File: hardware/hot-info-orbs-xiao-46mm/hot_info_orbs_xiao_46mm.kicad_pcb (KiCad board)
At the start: 2 copper layers, 224 x 47.8 mm, 13 parts, among them SW1 SW_Push, SW2 SW_Push, SW3 SW_Push, U2 XIAO ESP32-S3 Plus

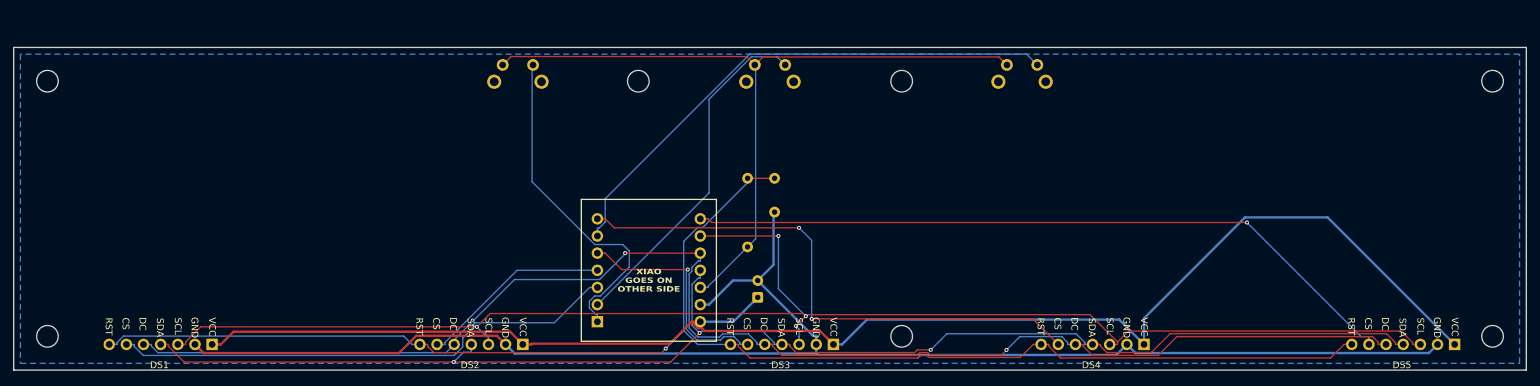
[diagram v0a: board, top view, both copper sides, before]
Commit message: 46 mm board rev 2.1: grown 5 mm at the top, posts on all seven holes
Placed in the Fusion overall assembly, the X0.2 board's top mounting holes
sat under the enclosure's top lip, so the top row hung from corner hangers.
Rejected shifting the board up: the displays are pinned by the bezel holes
and would move with it. Rejected keeping the hangers: Scott wants a post at
either end. So tools/grow_top.py grows the TOP edge 5 mm (the sockets fix
the bottom), moves the top-row holes, SW1-3 and labels with it, and the
board is re-routed from bare copper (300 tracks+vias, DRC clean).

Rev silk is 2.1 (Scott's number); it read X0.3 for a few minutes and that
zip was discarded, never ordered. fab/ gets a 2.1_run1 zip; the X0.2 zip
stays as the record and is marked superseded.

Fusion: main_body_front v4 (O6 posts + O2.9 pins on all seven holes,
hangers deleted, one body), overall assembly v4 (rev 2.1 STEP on the bezel
holes, xref refreshed). Interference enclosure vs PCB / display 5 clean.

TRAPS: the fusion-essentials active document flips between calls and reads
answer about the wrong doc; grow the edge, don't shift the board; KiCad
text must be set via pcbnew so the render_cache regenerates.

Co-Authored-By: Claude Fable 5.1 <noreply@anthropic.com>
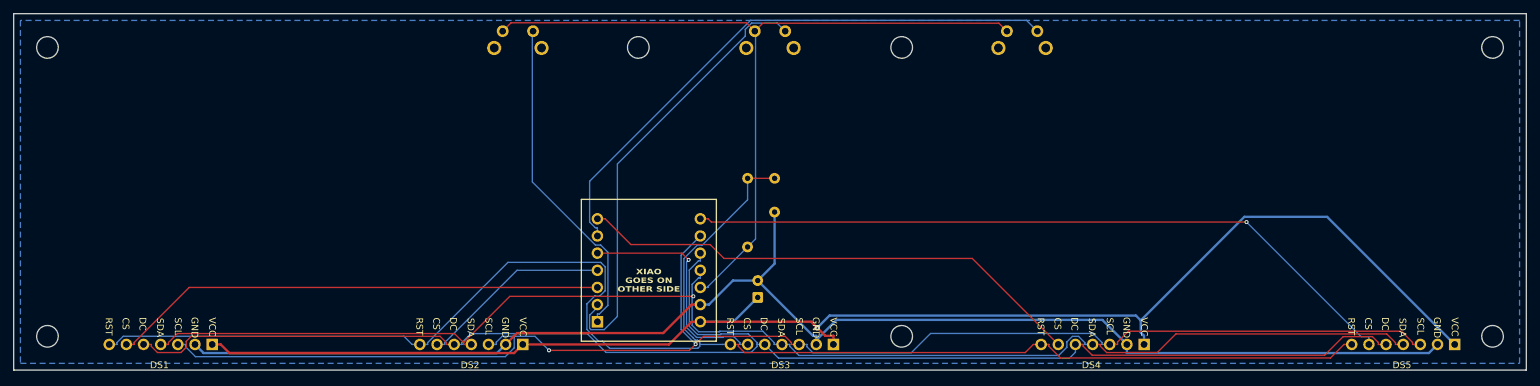
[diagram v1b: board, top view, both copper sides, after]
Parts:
- moved SW1 5.00 mm to (114.0, 59.6)
- moved SW2 5.00 mm to (151.3, 59.6)
- moved SW3 5.00 mm to (188.6, 59.6)
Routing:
- net /RST: track 222.9 -> 242.8 mm, vias 1 -> 0
- net GND: track 224.3 -> 209.4 mm
- net /SW2: track 51.6 -> 66.1 mm
- net /SCLK: track 224.8 -> 216.9 mm, vias 4 -> 2
- net /CS4: track 82.8 -> 76.0 mm, vias 2 -> 0
- net /SW3: track 79.7 -> 85.6 mm
- net /DC: track 211.9 -> 217.5 mm, vias 2 -> 0
- net /3V3: track 113.7 -> 118.7 mm
- net /CS1: track 75.8 -> 73.4 mm
- net /MOSI: track 208.1 -> 205.9 mm, vias 3 -> 1
- net /SW1: track 50.1 -> 49.0 mm
- net +5V: track 220.5 -> 220.0 mm, vias 0 -> 1
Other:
- board size 224 x 47.8 mm -> 224 x 52.8 mm
- board text added: "XIAO ESP32-S3 · rev 2.1 · 46 mm pitch"
- board text removed: "XIAO ESP32-S3 · rev X0.2 · 46 mm pitch"

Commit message: 46 mm board rev 2.3: XIAO 4 mm toward the bottom edge, passives beside it
Scott wants the USB-C jack as close to the enclosure wall as the board
allows without growing it or crowding the pins. tools/lower_xiao.py drops
U2 4.0 mm (the top of his 2-4 mm estimate): pad copper 2.31 mm from the
edge against a 0.5 rule, socket housings 1.9 mm inside it, USB-C face
0.6 mm past it. Rejected 2.73 mm (USB face flush with the edge, no silk
warnings) because the ask was "as much as possible"; the 3 warnings are
the footprint's own USB-C silk crossing the edge, which the fab trims.

C1 could not follow: DS3's back-side pin labels sit at y 101.9 and C1 was
already against them, so a 2.4 mm drop landed its 5V pad on the "DC"
label. It moves 3.2 mm sideways instead, courtyard 0.5 mm from the XIAO
socket, giving up the speculative castellation-pad margin. The 5V run is
9.25 mm pad to pad, the same as 2.1. C2 and R1 swap into one column above
C1, RST pads adjacent, so the long run is the 3V3 feed.

Re-routed from bare copper (284 tracks+vias, 0 unrouted), DRC 0 errors /
0 unconnected / 0 parity. New 2.3_run1 zip; the 2.1 zip stays as the
record. STEP overwritten in place, so the Fusion USB cutout built on 2.1
is 4 mm off until re-imported (noted in docs/ENCLOSURE.md). There is no
2.2. route_xiao.py now reruns Freerouting on a "stage interrupted" pass
with a non-empty SES, which its empty-file check missed.

Co-Authored-By: Claude Fable 5.1 <noreply@anthropic.com>
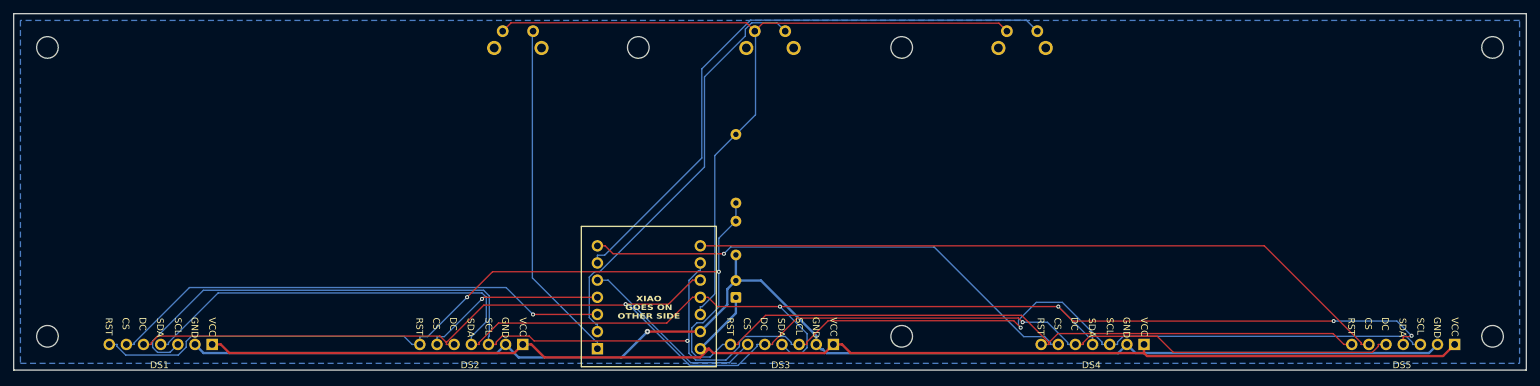
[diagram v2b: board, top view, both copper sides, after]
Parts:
- moved R1 16.8 mm to (144.0, 74.9), turned to -90 degrees
- moved C2 8.55 mm to (144.0, 87.7)
- moved U2 4.00 mm to (131.1, 99.0)
- moved C1 3.23 mm to (144.0, 99.0)
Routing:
- net /MOSI: track 205.9 -> 227.1 mm, vias 1 -> 4
- net +5V: track 220.0 -> 200.9 mm, vias 1 -> 0
- net /SCLK: track 216.9 -> 231.1 mm
- net /RST: track 242.8 -> 228.7 mm, vias 0 -> 2
- net GND: track 209.4 -> 202.5 mm, vias 0 -> 1
- net /CS3: track 34.4 -> 28.4 mm, vias 1 -> 0
- net /DC: track 217.5 -> 212.5 mm, vias 0 -> 2
- net /SW2: track 66.1 -> 62.3 mm
- net /SW3: track 85.6 -> 89.1 mm
- net /3V3: track 118.7 -> 122.2 mm
- net /SW1: track 49.0 -> 51.2 mm
- net /CS5: track 107.4 -> 105.2 mm, vias 1 -> 0
- net /CS1: track 73.4 -> 75.0 mm, vias 0 -> 1
- net /CS2: track 28.5 -> 27.3 mm, vias 0 -> 1
- net /CS4: track 76.0 -> 75.3 mm, vias 0 -> 1
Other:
- board text added: "XIAO ESP32-S3 · rev 2.3 · 46 mm pitch"
- board text removed: "XIAO ESP32-S3 · rev 2.1 · 46 mm pitch"

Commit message: 46 mm board rev 2.3 run 2: front GND pour + stitching vias in the two back-pour islands
Scott spotted two wide bare bands in the back pour (SW2 down past R1 to
the XIAO; DS1 to DS2 along the bottom edge). Measured with the fill redone
in memory and island removal off: removed islands of 283 and 211 mm2,
copper closed in by the SW2/SW3 pair and the 3V3 feed, and by the DS1
CS1/SCLK/MOSI bundle and the shared RST track. Removing them is correct,
so the fix is a connection: tools/stitch_islands.py puts a 0.8/0.3 GND via
in each island and pours the GND zone on F.Cu too.

Rejected "two vias only" (asked for, tried first): with no front copper the
island plus via is still floating and KiCad removes it again, DRC calls the
vias dangling. Rejected a front track from each via to a socket GND pin:
it would have to skirt the pin rows, and a front pour is normal on a
two-layer board. The front pour starves DS5's GND thermal to one spoke
(the +5V front track along the bottom runs under DS5 only); that pad's
spokes are turned 45 degrees on the board instance, rejected a solid
connection (hand soldering) and rerouting (everything would move).

DRC 0 errors / 3 warnings (USB-C silk over the edge, as before) / 0
unconnected / 0 parity. 16 vias. New zip 2.3_run2; run1 kept as the record
of the back-pour-only layout, not to be sent.

Co-Authored-By: Claude Fable 5.1 <noreply@anthropic.com>
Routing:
- net GND: vias 1 -> 3
- added copper zone on F.Cu, net GND
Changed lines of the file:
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@@
 			(remove_unused_layers no)
 			(net "GND")
+			(thermal_bridge_angle 45)
 		)
 		(pad "3" thru_hole oval
@@
 	)
 	(via
+		(at 68.699813 101.4584)
+		(size 0.8)
+		(drill 0.3)
+		(layers "F.Cu" "B.Cu")
+		(net "GND")
+	)
+	(via
+		(at 143.100652 68.130134)
+		(size 0.8)
+		(drill 0.3)
+		(layers "F.Cu" "B.Cu")
+		(net "GND")
+	)
+	(via
 		(at 130.8936 104.08)
 		(size 0.8)
@@
 	(zone
 		(net "GND")
-		(layer "B.Cu")
+		(layers "F.Cu" "B.Cu")
 		(name "GND")
 		(hatch edge 0.5)
